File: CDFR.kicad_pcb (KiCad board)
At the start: 2 copper layers, 56 x 64.9 mm, 11 parts, among them J1 Conn_01x03, J2 Conn_01x03, J3 Conn_01x03, J4 Conn_01x03, J5 Conn_01x03, J6 Conn_01x02_Socket, J7 Screw_Terminal_01x02, U1 RASPBERRY_PI_3_MODEL_B_, U2 YAAJ_DCDC_StepDown_LM2596

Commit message: Add files via upload
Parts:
- moved J5 71.8 mm to (123.0, 33.0), turned to 180 degrees
- moved J1 67.4 mm to (110.5, 41.0), turned to -90 degrees
- moved J2 54.4 mm to (110.5, 52.5), turned to -90 degrees
- moved J3 48.6 mm to (110.5, 64.0), turned to -90 degrees
- moved J4 47.4 mm to (110.5, 75.5), turned to -90 degrees
- moved J6 19.1 mm to (148.0, 89.0), turned to 90 degrees
- moved R2 10.9 mm to (148.4, 48.8), turned to 0 degrees
- moved J7 4.42 mm to (133.0, 39.0)
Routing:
- net unconnected-(U1-SHIELD-PadS1): track 0.00 -> 222.6 mm
- net GND: track 167.1 -> 12.3 mm
- net /I2C_SDA: track 121.9 -> 201.3 mm
- net +3.3V: track 11.6 -> 38.7 mm
- net Net-(J7-Pin_2): track 0.00 -> 23.3 mm
- net /I2C_CLK: track 126.8 -> 111.7 mm
- net Net-(U2-Vout): track 59.8 -> 73.0 mm
- net Net-(J7-Pin_1): track 0.00 -> 12.7 mm
- net Net-(J6-Pin_1): track 12.3 -> 20.5 mm
- added copper zone on B.Cu, net GND
- added copper zone on F.Cu, net GND

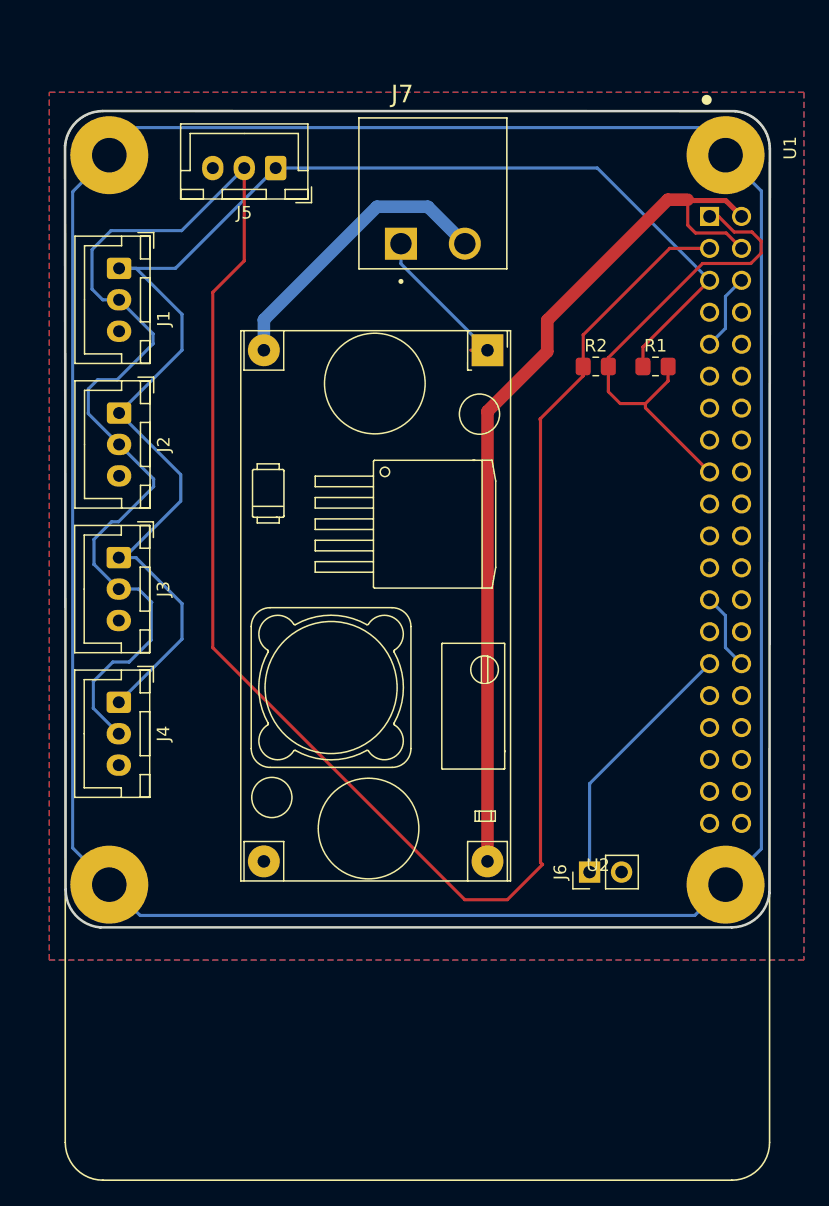
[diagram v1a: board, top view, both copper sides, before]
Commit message: ajout lidar et antiRerse voltage
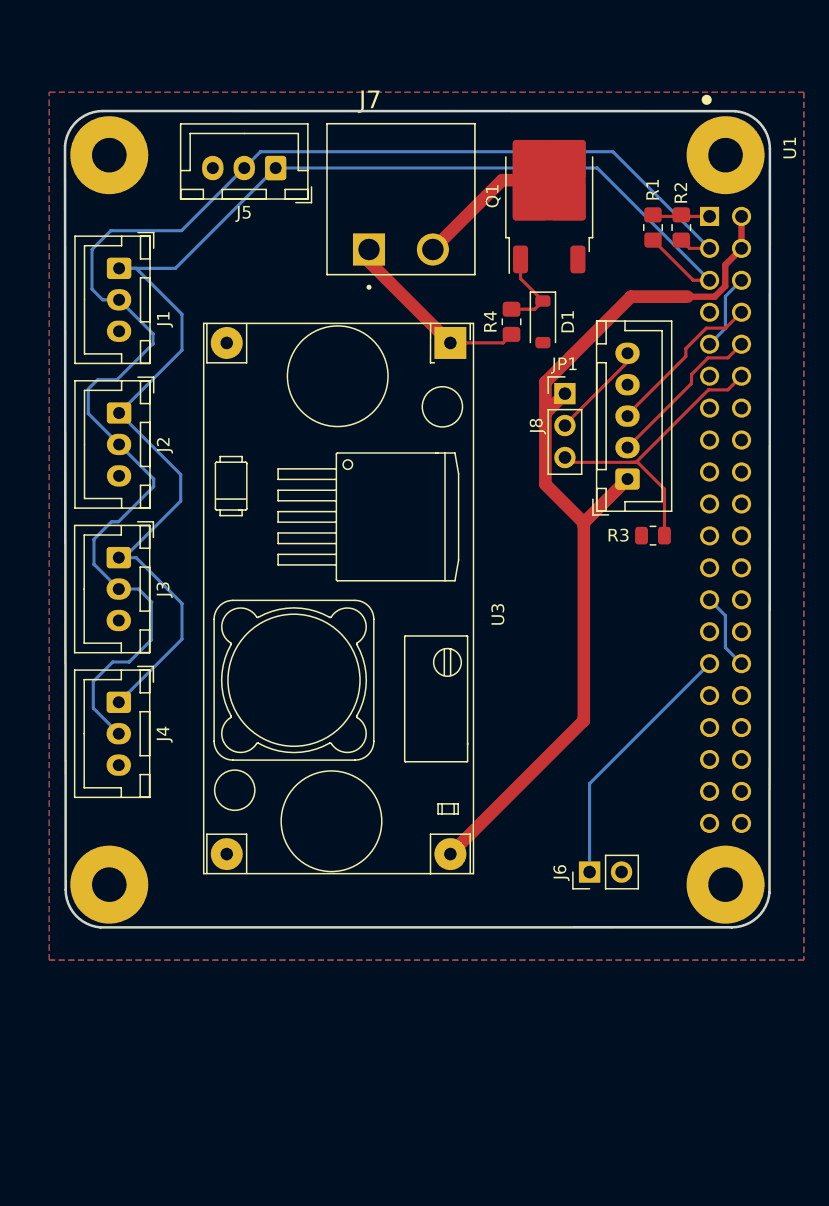
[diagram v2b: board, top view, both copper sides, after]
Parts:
- removed U2: YAAJ_DCDC_StepDown_LM2596, emprient2:YAAJ_DCDC_StepDown_LM2596
- added D1: D_Zener, Diode_SMD:D_SOD-123, F.Cu at (144.2, 45.2)
- added J8: Conn_01x05_Socket, Connector_JST:JST_XH_B5B-XH-A_1x05_P2.50mm_Vertical, F.Cu at (151.0, 57.8)
- added JP1: Jumper_3_Open, Connector_PinHeader_2.54mm:PinHeader_1x03_P2.54mm_Vertical, F.Cu at (146.0, 51.0)
- added Q1: Q_NMOS_GDS, Package_TO_SOT_SMD:TO-252-2, F.Cu at (144.8, 35.2)
- added R3: 100M, Resistor_SMD:R_0805_2012Metric, F.Cu at (153.0, 62.2)
- added R4: 56k, Resistor_SMD:R_0805_2012Metric_Pad1.20x1.40mm_HandSolder, F.Cu at (141.8, 45.2)
- added U3: YAAJ_DCDC_StepDown_LM2596, LM2596:YAAJ_DCDC_StepDown_LM2596, F.Cu at (136.9, 46.9)
- U1: footprint emprient:MODULE_RASPBERRY_PI_3_MODEL_B_ -> raspberryPi:EmpreintPourShiel_RaspberryPi3B
- moved R2 13.0 mm to (155.2, 37.8), turned to 90 degrees
- moved R1 11.1 mm to (153.0, 37.8), turned to 90 degrees
- moved J7 2.58 mm to (130.4, 39.5)
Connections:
- net Net-(U2-Vout) renamed +5V
- U1 pad 10: unconnected-(U1-GPIO15/RXD0-Pad10) -> Net-(J8-Pin_2)
- U1 pad 12: unconnected-(U1-GPIO18/GPIO_GEN1-Pad12) -> MotorControl
- U1 pad 17: +3.3V -> unconnected-(U1-3V3-Pad17)
- U1 pad 8: unconnected-(U1-GPIO14/TXD0-Pad8) -> Net-(J8-Pin_3)
- U1 pad S1: unconnected-(U1-SHIELD-PadS1) -> GND
- U1 pad S2: unconnected-(U1-SHIELD-PadS1) -> GND
- U1 pad S3: unconnected-(U1-SHIELD-PadS1) -> GND
- U1 pad S4: unconnected-(U1-SHIELD-PadS1) -> GND
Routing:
- net unconnected-(U1-SHIELD-PadS1): track 222.6 -> 0.00 mm
- net /I2C_SDA: track 201.3 -> 113.2 mm
- net +3.3V: track 38.7 -> 4.55 mm
- net MotorControl: track 0.00 -> 24.3 mm
- net Net-(J8-Pin_3): track 0.00 -> 12.9 mm
- net Net-(J8-Pin_2): track 0.00 -> 12.9 mm
- net Net-(J7-Pin_2): track 23.3 -> 11.5 mm
- net Net-(J8-Pin_5): track 0.00 -> 7.81 mm
- net Net-(D1-K): track 0.00 -> 6.82 mm
- net /I2C_CLK: track 111.7 -> 108.5 mm
- net Net-(J7-Pin_1): track 12.7 -> 15.3 mm
- net +5V: track 73.0 -> 73.8 mm

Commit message: ajout i2c power
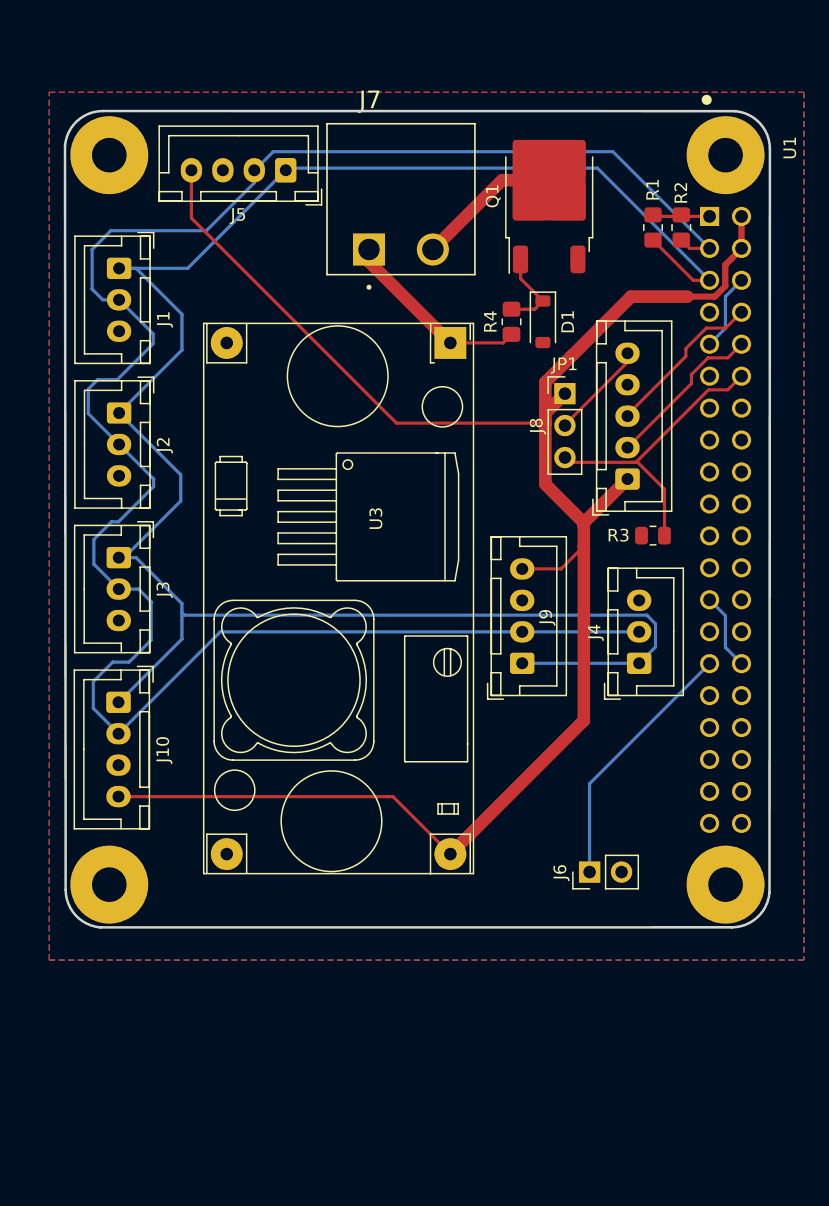
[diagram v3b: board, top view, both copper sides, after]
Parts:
- added J10: Conn_01x04, Connector_JST:JST_XH_B4B-XH-A_1x04_P2.50mm_Vertical, F.Cu at (110.5, 75.5)
- added J9: Conn_01x04, Connector_JST:JST_XH_B4B-XH-A_1x04_P2.50mm_Vertical, F.Cu at (142.6, 72.4)
- J5: value Conn_01x03 -> Conn_01x04; footprint Connector_JST:JST_XH_B3B-XH-A_1x03_P2.50mm_Vertical -> Connector_JST:JST_XH_B4B-XH-A_1x04_P2.50mm_Vertical
- moved J4 41.5 mm to (151.9, 72.4), turned to 90 degrees
- moved J5 0.82 mm to (123.8, 33.2)
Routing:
- net +5V: track 73.8 -> 146.5 mm
- net /I2C_CLK: track 108.5 -> 159.5 mm
- net /I2C_SDA: track 113.2 -> 158.5 mm

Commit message: Mise à jour référence
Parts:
- renumbered J10 to J10_I2C1, J1 to J1_I2C1, J2 to J2_I2C1, J3 to J3_I2C1, J4 to J4_I2C1, J5 to J5_I2C1, J8 to J8_UART0, J9 to J9_I2C1

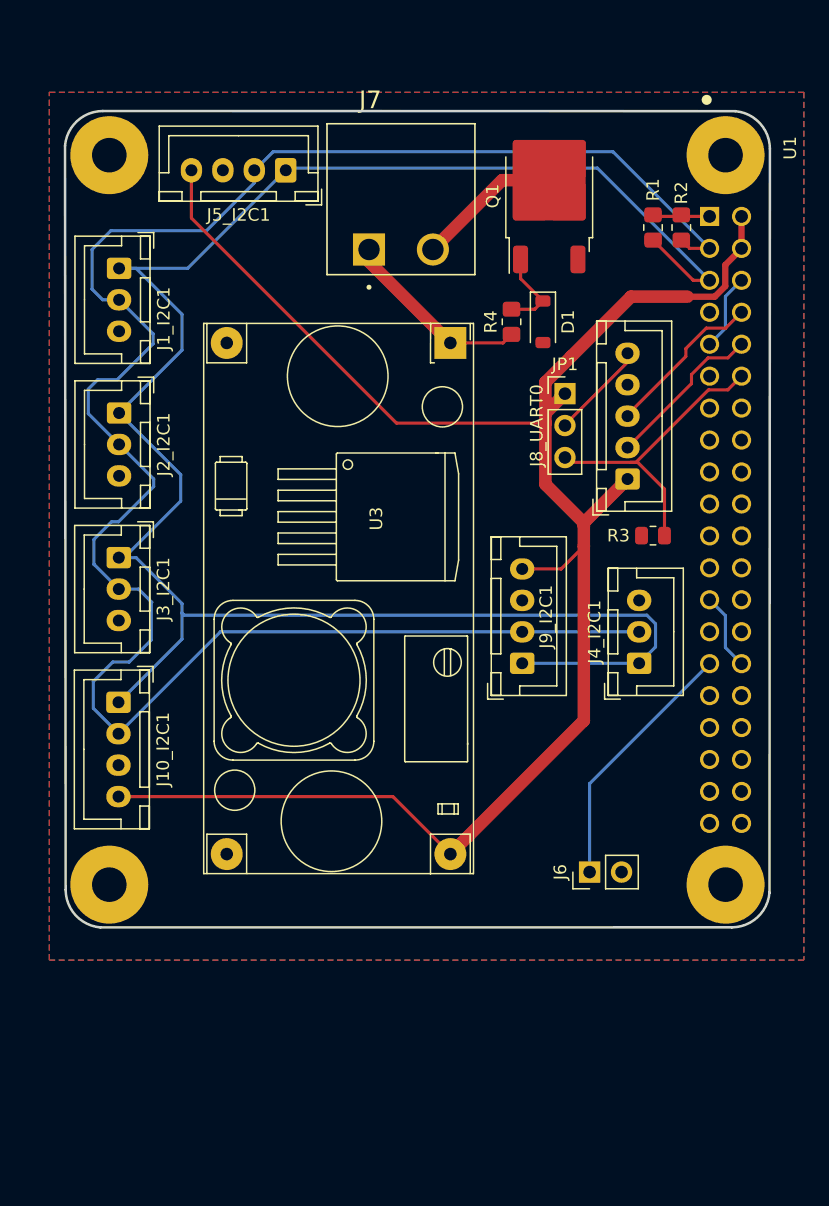
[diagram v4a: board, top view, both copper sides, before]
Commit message: TracoPower addition
Ajout traco power
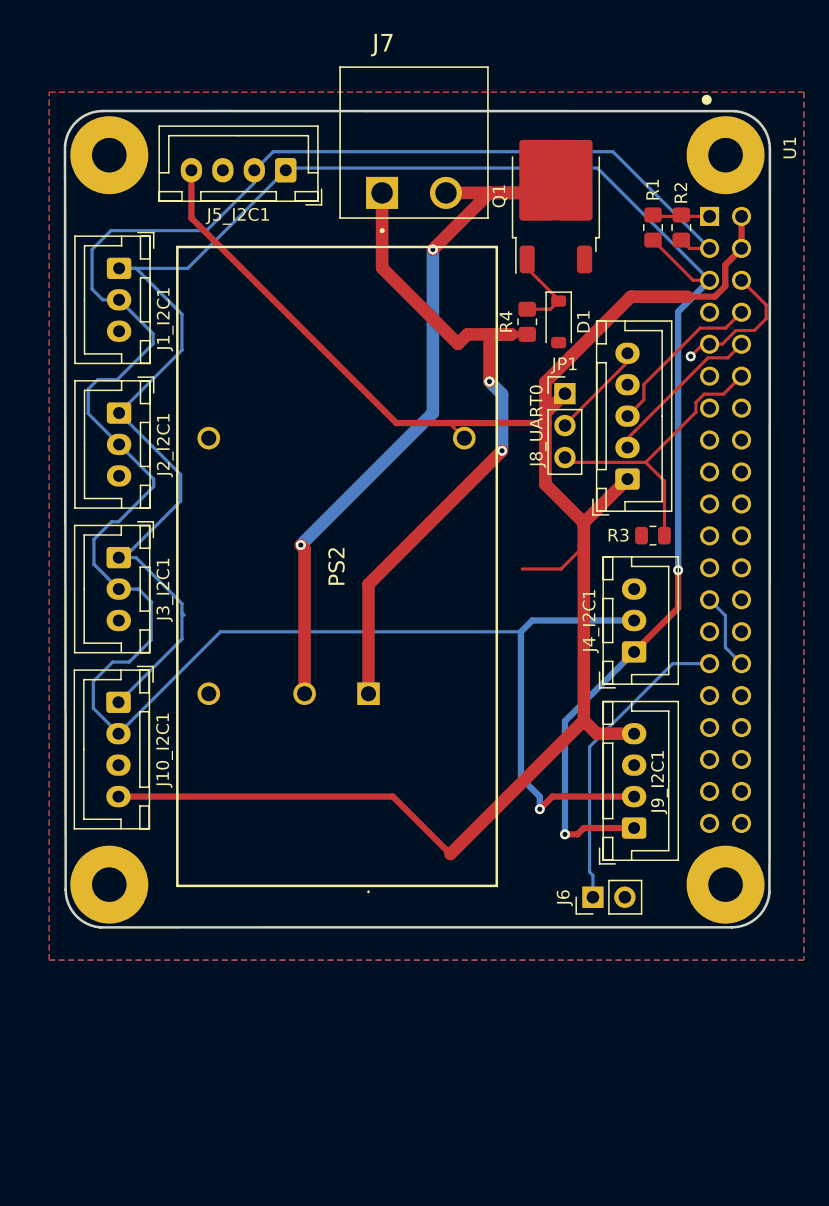
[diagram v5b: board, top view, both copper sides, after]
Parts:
- removed U3: YAAJ_DCDC_StepDown_LM2596, LM2596:YAAJ_DCDC_StepDown_LM2596
- added PS2: TEN_15-2411WI, SamacSys_Parts:TEN152411WI, F.Cu at (130.4, 74.8)
- moved J9_I2C1 15.8 mm to (151.5, 85.5)
- moved J7 4.62 mm to (131.5, 35.0)
- moved J6 2.02 mm to (148.2, 91.0)
- moved D1 1.25 mm to (145.5, 45.2)
- moved R4 1.25 mm to (143.0, 45.2)
- moved J4_I2C1 0.98 mm to (151.5, 71.5)
- moved Q1 0.53 mm to (145.3, 35.2)
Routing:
- net Net-(J7-Pin_2): track 11.5 -> 58.1 mm, vias 0 -> 2
- net Net-(J7-Pin_1): track 15.3 -> 55.4 mm, vias 0 -> 2
- net /I2C_SDA: track 158.5 -> 181.2 mm, vias 0 -> 1
- net +5V: track 146.5 -> 153.4 mm
- net GND: track 12.3 -> 17.2 mm, vias 0 -> 1
- net Net-(J6-Pin_1): track 20.5 -> 24.3 mm
- net /I2C_CLK: track 159.5 -> 163.3 mm, vias 0 -> 2

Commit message: Ajout porte fusible
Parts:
- added F1: 0154004.DR, FuseHolder:FUSE_0154004.DR, F.Cu at (144.5, 69.5)
- PS2: footprint SamacSys_Parts:TEN152411WI -> TEN152411:TEN152411WI
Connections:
- PS2 pad 2: Net-(J7-Pin_2) -> Net-(PS2--VIN_(GND))
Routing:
- net Net-(PS2--VIN_(GND)): track 0.00 -> 24.0 mm
- net Net-(J7-Pin_2): track 58.1 -> 50.1 mm
- net +5V: track 153.4 -> 151.7 mm
